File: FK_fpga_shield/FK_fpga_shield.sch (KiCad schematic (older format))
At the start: 12 parts, among them J1 USB_B_Mini, J2 Conn_02x20_Odd_Even, J3 Conn_02x20_Odd_Even, J4 molex-51382-0400-microclasp, U1 FT232RL, U2 nvt2010pw

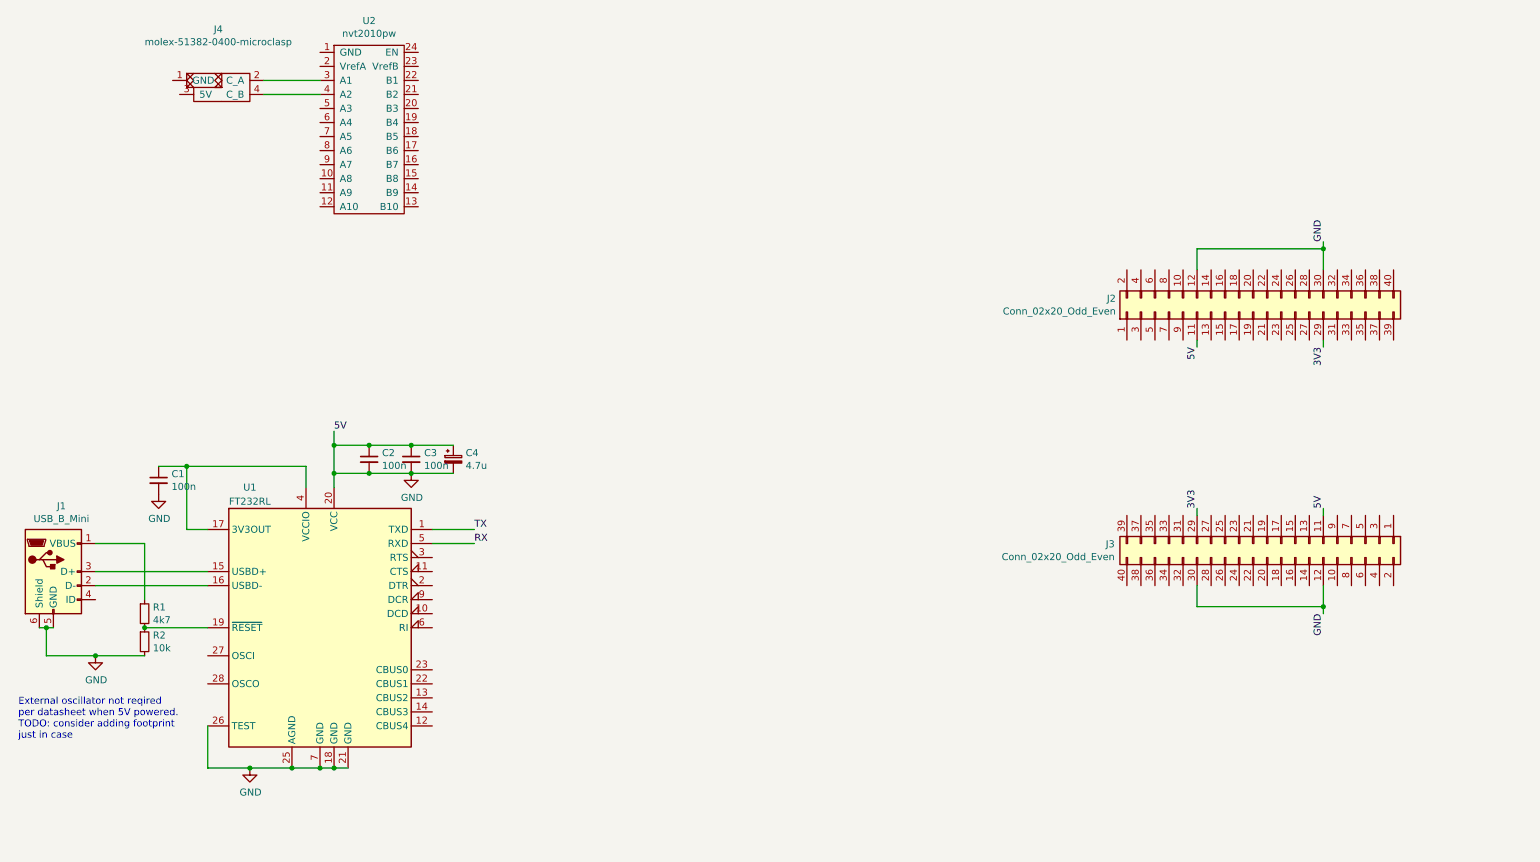
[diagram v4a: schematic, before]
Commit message: single level shifter schema
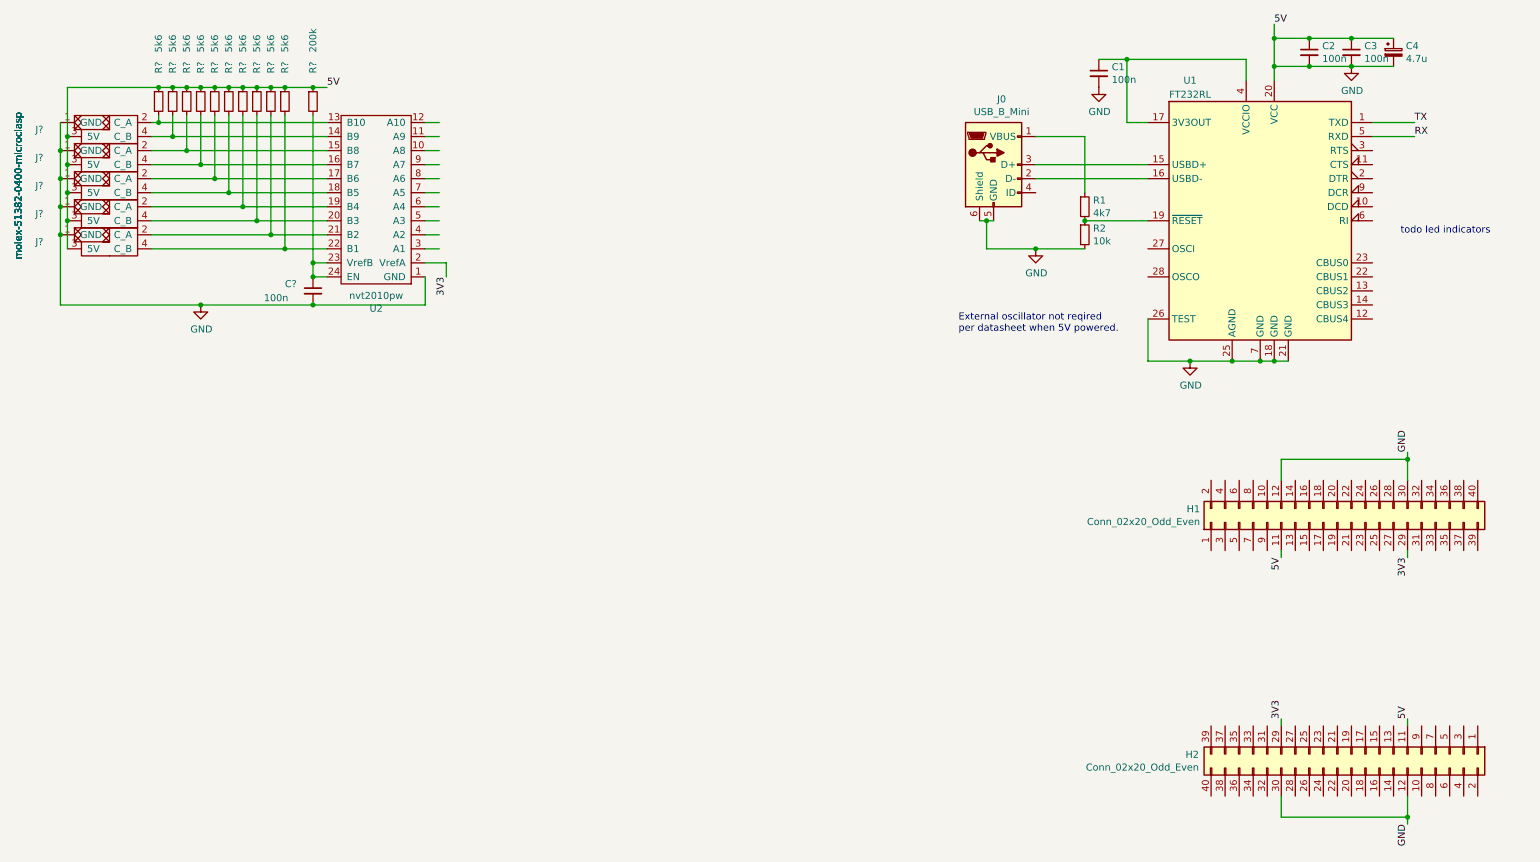
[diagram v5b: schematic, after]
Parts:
- removed J4: molex-51382-0400-microclasp, FK_fpga_shield_custom_footprints:Molex_MicroClasp_55935-0410_1x04_P2.00mm_Horizontal_3DMODEL, symbol FK_fpga_shield_custom_symbols:molex-51382-0400-microclasp
- added C?: 100n, Capacitor_SMD:C_0805_2012Metric_Pad1.15x1.40mm_HandSolder, symbol Device:C_Small
- added J? (x5): molex-51382-0400-microclasp, symbol FK_fpga_shield_custom_symbols:molex-51382-0400-microclasp
- added R? (x10): 5k6, Resistor_SMD:R_0805_2012Metric_Pad1.15x1.40mm_HandSolder, symbol Device:R_Small
- added R?: 200k, Resistor_SMD:R_0805_2012Metric_Pad1.15x1.40mm_HandSolder, symbol Device:R_Small
- renumbered J2 to H1, J3 to H2, J1 to J0
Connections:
- wire segments 46 -> 116
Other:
- note added: "External oscillator not reqired\nper datasheet when 5V powered.\n"
- note added: "todo led indicators"
- note removed: "External oscillator not reqired\nper datasheet when 5V powered.\nTODO: consider adding footprint\njust in case"
- moved on the sheet: C1, C2, C3, C4, H1, H2, J0, R1, R2, U1, U2

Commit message: WIP fpga shield layout
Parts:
- added C10, C11, C6, C7, C8, C9: 100n, Capacitor_SMD:C_0805_2012Metric_Pad1.15x1.40mm_HandSolder, symbol Device:C_Small
- added J10, J11, J12, J13, J14, J15, J16, J17, J18, J19, J20, J21, J22, J23, J24, J25, J26, J27, J28, J29, J30, J31, J32, J33, J34, J35, J6, J7, J8, J9: molex-51382-0400-microclasp, FK_fpga_shield_custom_footprints:Molex_MicroClasp_55935-0410_1x04_P2.00mm_Horizontal_3DMODEL, symbol FK_fpga_shield_custom_symbols:molex-51382-0400-microclasp
- added R10, R11, R12, R14, R15, R16, R17, R19, R20, R21, R22, R24, R25, R26, R27, R29, R30, R31, R32, R34, R35, R36, R37, R39, R4, R40, R41, R42, R44, R45, R46, R47, R49, R5, R50, R51, R52, R58, R59, R6, R60, R61, R62, R63, R64, R65, R66, R67, R68, R69, R7, R70, R71, R72, R73, R74, R75, R76, R77, R9: 5k6, Resistor_SMD:R_0805_2012Metric_Pad1.15x1.40mm_HandSolder, symbol Device:R_Small
- added R54, R55, R56, R57, R78, R79: 200k, Resistor_SMD:R_0805_2012Metric_Pad1.15x1.40mm_HandSolder, symbol Device:R_Small
- added U3, U4, U5, U6, U7, U8: nvt2010pw, Package_SO:TSSOP-24_4.4x7.8mm_P0.65mm, symbol FK_fpga_shield_custom_symbols:nvt2010pw
- C1, C2, C3, C4: footprint (none) -> Capacitor_SMD:C_0805_2012Metric_Pad1.15x1.40mm_HandSolder
- J1, J2, J3, J4, J5: renamed from J?; footprint (none) -> FK_fpga_shield_custom_footprints:Molex_MicroClasp_55935-0410_1x04_P2.00mm_Horizontal_3DMODEL
- R1, R2: footprint (none) -> Resistor_SMD:R_0805_2012Metric_Pad1.15x1.40mm_HandSolder
- U2: footprint (none) -> Package_SO:TSSOP-24_4.4x7.8mm_P0.65mm
- gave numbers to parts that had none: 12
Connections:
- net labels added: 1a, 1b, 2a, 2b, 3a, 3b, 4a, 4b, 5a, 5b
- wire segments 116 -> 539
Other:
- moved on the sheet: C1, C2, C3, C4, C5, H1, H2, J0, J1, J2, J3, J4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

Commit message: wip lazyour (mapped to header)
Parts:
- renumbered J25 to J21, J24 to J22, J22 to J24, J21 to J25, J30 to J26, J29 to J27, J27 to J29, J26 to J30, J35 to J31, J34 to J32, J32 to J34, J31 to J35
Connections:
- net labels added: 10a, 10b, 11a, 11b, 12a, 12b, 13a, 13b, 14a, 14b, 15a, 15b, 16a, 16b, 17a, 17b, 18a, 18b, 19a, 19b, 20a, 20b, 21a, 21b, 22a, 22b, 23a, 23b, 24a, 24b, 25a, 25b, 26a, 26b, 27a, 27b, 28a, 28b, 29a, 29b, 30a, 30b, 31a, 31b, 32a, 32b, 33a, 33b, 34a, 34b, 35a, 35b, 6a, 6b, 7a, 7b, 8a, 8b, 9a, 9b

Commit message: wip
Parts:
- added J?: Barrel_Jack, symbol Connector:Barrel_Jack
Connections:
- net 5V: now also J?.1
- net GND: now also J?.2
- net RX: now also H2.39 (Pin_39); no longer H2.40 (Pin_40)
- net TX: now also H2.40 (Pin_40); no longer H2.39 (Pin_39)
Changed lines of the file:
@@
 	1    0    0    -1
 $EndComp
+Text Label 12950 6450 1    50   ~ 0
+RX
 Text Label 12950 6950 3    50   ~ 0
-RX
-Text Label 12950 6450 1    50   ~ 0
 TX
 Text Label 3550 2050 0    50   ~ 0
@@
 Text Label 13050 6950 3    50   ~ 0
 35a
+$Comp
+L Connector:Barrel_Jack J?
+U 1 1 61D44947
+P 10300 6600
+F 0 "J?" H 10357 6925 50  0000 C CNN
+F 1 "Barrel_Jack" H 10357 6834 50  0000 C CNN
+F 2 "" H 10350 6560 50  0001 C CNN
+F 3 "~" H 10350 6560 50  0001 C CNN
+	1    10300 6600
+	1    0    0    -1
+$EndComp
+$Comp
+L power:GND #PWR?
+U 1 1 61D45B36
+P 10750 6700
+F 0 "#PWR?" H 10750 6450 50  0001 C CNN
+F 1 "GND" H 10755 6527 50  0000 C CNN
+F 2 "" H 10750 6700 50  0001 C CNN
+F 3 "" H 10750 6700 50  0001 C CNN
+	1    10750 6700
+	1    0    0    -1
+$EndComp
+Wire Wire Line
+	10600 6700 10750 6700
+Text Label 10750 6500 0    50   ~ 0
+5V
+Wire Wire Line
+	10600 6500 10750 6500
 $EndSCHEMATC
